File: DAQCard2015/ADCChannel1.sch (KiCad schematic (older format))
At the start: 50 parts, among them U1 LTC6403, U2 AD9219, U3 LTC6403, U4 LTC6403, U5 LTC6403

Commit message: Replaces single ample with 4-channel varients. Greatly reducing part count
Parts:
- removed C1, C15, C16: .01uF, symbol C
- removed C12, C13, C14, C17, C18, C19, C20, C21, C22: C, symbol C
- removed C8: 2.2uF, symbol CP
- removed C9: .1uF, symbol C
- removed R1, R13, R14: Rt, symbol R
- removed R11, R12, R19, R20, R21, R22: Rf, symbol R
- removed R15, R16, R17, R18, R2, R3: Ri, symbol R
- removed R23: 2.7k, symbol R
- removed R24: 1k, symbol R
- removed U1, U3, U4, U5: LTC6403, symbol LTC6403
- removed U2: AD9219, symbol AD9219
- added C8: .1uF, symbol C
- added C9: 2.2uF, symbol CP
- added R4: Rt, symbol R
- added RP1: R_PACK8, symbol R_PACK8
- added RP2, RP3: Rf, symbol R_PACK4
- added U2: THS4524IDBTR, symbol THS4524IDBTR
- added U3: AD9219, symbol AD9219
- C11: value .01uF -> .1uF
- C2, C3: value .1uF -> C
- C5: value C -> .01uF
- C6: value C -> .1uF
- R10: value Ri -> 10k
- R5, R6: value Rf -> Rt
- R7: value 10k -> Rt
- R8: value Rt -> 2.7k
- R9: value Ri -> 1k
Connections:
- net labels added: 3V3ana, VOCM
- net labels removed: 3V3, Vocm
- wire segments 178 -> 192
- no-connect marks 12 -> 4

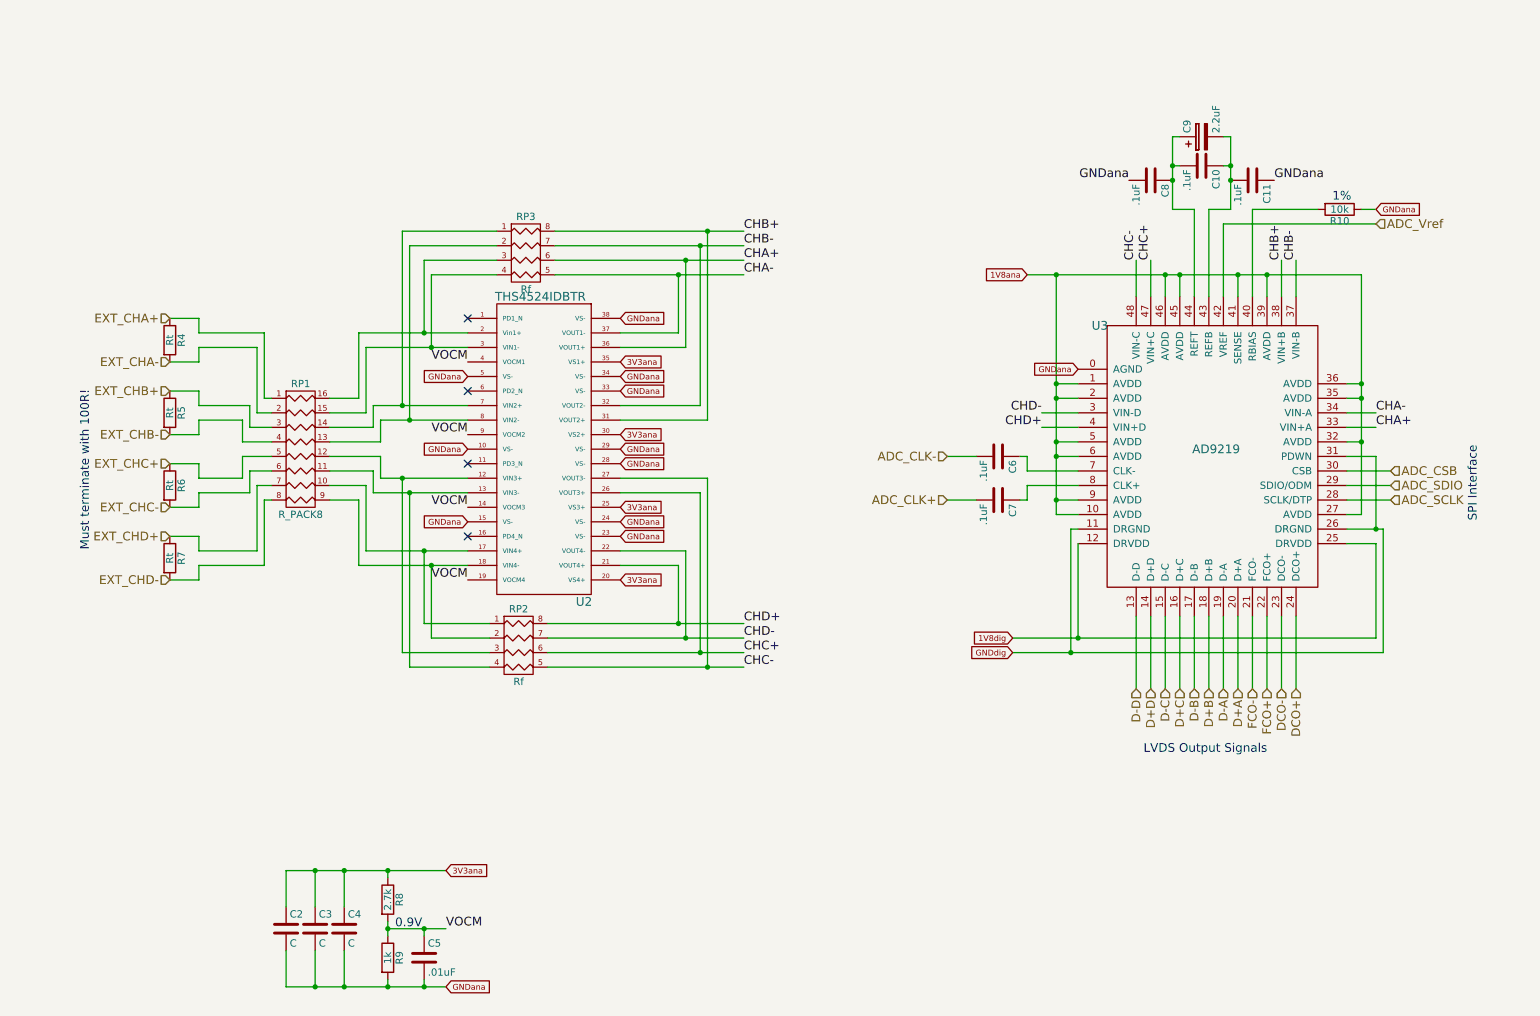
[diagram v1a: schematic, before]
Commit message: Finishes initial version of schematic(mostly). And adds a whole bunch of new footprints!
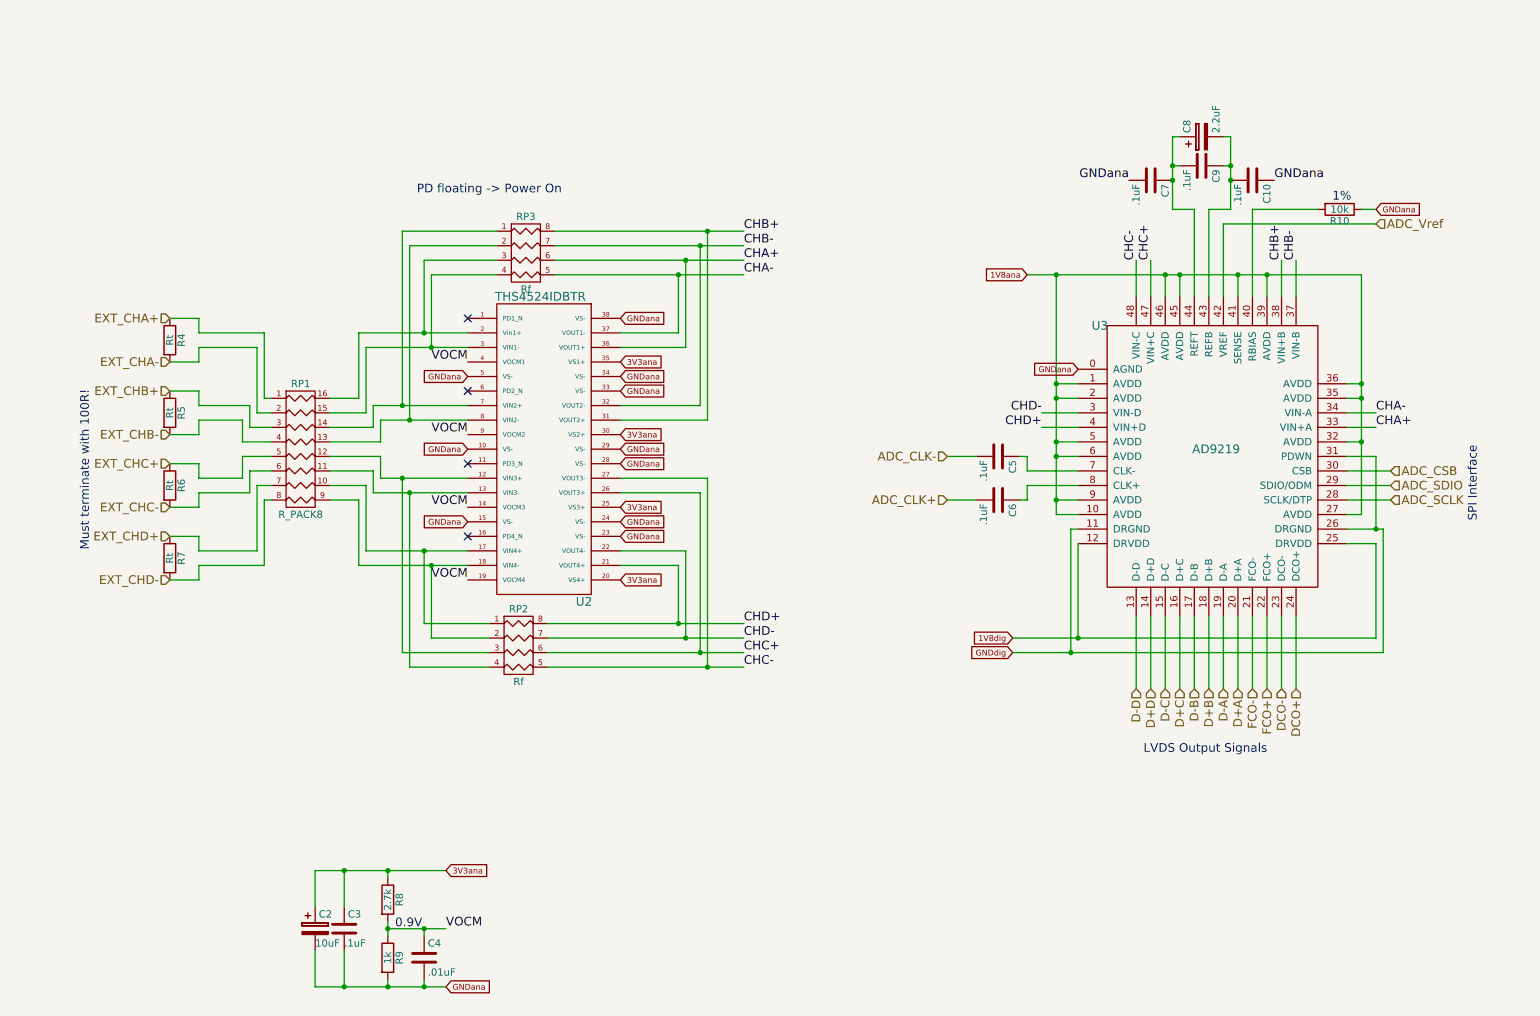
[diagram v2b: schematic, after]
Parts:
- removed C11, C8: .1uF, symbol C
- removed C2: C, symbol C
- removed C9: 2.2uF, symbol CP
- added C2: 10uF, extras:SMD_Cap_3mmDia, symbol CP
- added C8: 2.2uF, extras:SMD_Cap_3mmDia, symbol CP
- added C9: .1uF, Capacitors_SMD:C_0603, symbol C
- C10, C6, C7: footprint (none) -> Capacitors_SMD:C_0603
- C3: value C -> .1uF; footprint (none) -> Capacitors_SMD:C_0603
- C4: value C -> .01uF; footprint (none) -> Capacitors_SMD:C_0603
- C5: value .01uF -> .1uF; footprint (none) -> Capacitors_SMD:C_0603
- R10, R4, R5, R6, R7, R8, R9: footprint (none) -> Resistors_SMD:R_0603
- RP1: footprint (none) -> extras:R8_MNR18
- RP2, RP3: footprint (none) -> extras:R4-MNR04
- U2: footprint (none) -> Housings_SSOP:TSSOP-38_4.4x9.7mm_Pitch0.5mm
- U3: footprint (none) -> SMD_Packages:QFN-48-1EP
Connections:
- net 3V3ana: now also C2.1; no longer C4.1
- net ADC_CLK+: now also C6.2; no longer C7.2
- net ADC_CLK-: now also C5.2; no longer C6.2
- net GNDana: now also C10.1, C7.2, C2.2; no longer C5.2
- net VOCM: now also C4.1; no longer C5.1
- net at U3.8 (CLK+): now also C6.1; no longer C7.1
- net at U3.43 (REFB): now also C10.2, C8.2, C9.1; no longer C10.1
- net at U3.44 (REFT): now also C7.1, C8.1, C9.2; no longer C10.2
- net at U3.7 (CLK-): now also C5.1; no longer C6.1
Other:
- note added: "PD floating -> Power On"
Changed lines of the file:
@@
 $Comp
 L AD9219 U3
-U 1 1 55CFF5AD
+U 1 1 55CB5758
 P 9050 3700
 F 0 "U3" H 8250 4650 60  0000 C CNN
 F 1 "AD9219" H 9050 3800 60  0000 C CNN
-F 2 "" H 8650 3700 60  0000 C CNN
+F 2 "SMD_Packages:QFN-48-1EP" H 8650 3700 60  0001 C CNN
 F 3 "" H 8650 3700 60  0000 C CNN
 	1    9050 3700
@@
 $Comp
 L R R8
-U 1 1 55CFF5F5
+U 1 1 55CB5786
 P 3350 6700
 F 0 "R8" V 3430 6700 50  0000 C CNN
 F 1 "2.7k" V 3350 6700 50  0000 C CNN
-F 2 "" V 3280 6700 30  0000 C CNN
+F 2 "Resistors_SMD:R_0603" V 3280 6700 30  0001 C CNN
 F 3 "" H 3350 6700 30  0000 C CNN
 	1    3350 6700
@@
 $Comp
 L R R9
-U 1 1 55CFF5DE
+U 1 1 55CB577C
 P 3350 7100
 F 0 "R9" V 3430 7100 50  0000 C CNN
 F 1 "1k" V 3350 7100 50  0000 C CNN
-F 2 "" V 3280 7100 30  0000 C CNN
+F 2 "Resistors_SMD:R_0603" V 3280 7100 30  0001 C CNN
 F 3 "" H 3350 7100 30  0000 C CNN
 	1    3350 7100
@@
 Must terminate with 100R!
 $Comp
-L C C2
-U 1 1 55CFF5C9
-P 2650 6900
-F 0 "C2" H 2675 7000 50  0000 L CNN
-F 1 "C" H 2675 6800 50  0000 L CNN
-F 2 "" H 2688 6750 30  0000 C CNN
-F 3 "" H 2650 6900 60  0000 C CNN
-	1    2650 6900
-	1    0    0    -1
-$EndComp
-$Comp
 L C C3
-U 1 1 55CFF5B5
-P 2850 6900
-F 0 "C3" H 2875 7000 50  0000 L CNN
-F 1 "C" H 2875 6800 50  0000 L CNN
-F 2 "" H 2888 6750 30  0000 C CNN
-F 3 "" H 2850 6900 60  0000 C CNN
-	1    2850 6900
-	1    0    0    -1
-$EndComp
-$Comp
-L C C4
-U 1 1 55CFF5BB
+U 1 1 55CB575C
 P 3050 6900
-F 0 "C4" H 3075 7000 50  0000 L CNN
-F 1 "C" H 3075 6800 50  0000 L CNN
-F 2 "" H 3088 6750 30  0000 C CNN
+F 0 "C3" H 3075 7000 50  0000 L CNN
+F 1 ".1uF" H 3050 6800 50  0000 L CNN
+F 2 "Capacitors_SMD:C_0603" H 3088 6750 30  0001 C CNN
 F 3 "" H 3050 6900 60  0000 C CNN
 	1    3050 6900
@@
 ADC_SCLK
 $Comp
-L C C6
-U 1 1 55CFF5C6
+L C C5
+U 1 1 55CB5765
 P 7550 3650
-F 0 "C6" H 7575 3750 50  0000 L CNN
+F 0 "C5" H 7575 3750 50  0000 L CNN
 F 1 ".1uF" H 7575 3550 50  0000 L CNN
-F 2 "" H 7588 3500 30  0000 C CNN
+F 2 "Capacitors_SMD:C_0603" H 7588 3500 30  0001 C CNN
 F 3 "" H 7550 3650 60  0000 C CNN
 	1    7550 3650
@@
 $EndComp
 $Comp
-L C C7
-U 1 1 55CE4061
+L C C6
+U 1 1 55CB5746
 P 7550 3950
-F 0 "C7" H 7575 4050 50  0000 L CNN
+F 0 "C6" H 7575 4050 50  0000 L CNN
 F 1 ".1uF" H 7575 3850 50  0000 L CNN
-F 2 "" H 7588 3800 30  0000 C CNN
+F 2 "Capacitors_SMD:C_0603" H 7588 3800 30  0001 C CNN
 F 3 "" H 7550 3950 60  0000 C CNN
 	1    7550 3950
@@
 DCO+
 $Comp
-L C C11
-U 1 1 55CFF5FE
+L C C10
+U 1 1 55CB578F
 P 9300 1750
-F 0 "C11" H 9325 1850 50  0000 L CNN
+F 0 "C10" H 9325 1850 50  0000 L CNN
 F 1 ".1uF" H 9325 1650 50  0000 L CNN
-F 2 "" H 9338 1600 30  0000 C CNN
+F 2 "Capacitors_SMD:C_0603" H 9338 1600 30  0001 C CNN
 F 3 "" H 9300 1750 60  0000 C CNN
 	1    9300 1750
@@
 $EndComp
 $Comp
-L C C8
-U 1 1 55CFF5CE
+L C C7
+U 1 1 55CB5768
 P 8600 1750
-F 0 "C8" H 8625 1850 50  0000 L CNN
+F 0 "C7" H 8625 1850 50  0000 L CNN
 F 1 ".1uF" H 8625 1650 50  0000 L CNN
-F 2 "" H 8638 1600 30  0000 C CNN
+F 2 "Capacitors_SMD:C_0603" H 8638 1600 30  0001 C CNN
 F 3 "" H 8600 1750 60  0000 C CNN
 	1    8600 1750
@@
 $EndComp
 $Comp
-L C C10
-U 1 1 55CFF5D5
+L C C9
+U 1 1 55CB576F
 P 8950 1650
-F 0 "C10" H 8975 1750 50  0000 L CNN
+F 0 "C9" H 8975 1750 50  0000 L CNN
 F 1 ".1uF" H 8975 1550 50  0000 L CNN
-F 2 "" H 8988 1500 30  0000 C CNN
+F 2 "Capacitors_SMD:C_0603" H 8988 1500 30  0001 C CNN
 F 3 "" H 8950 1650 60  0000 C CNN
 	1    8950 1650
@@
 GNDana
 $Comp
-L CP C9
-U 1 1 55CFF600
+L CP C8
+U 1 1 55CB5792
 P 8950 1450
-F 0 "C9" H 8975 1550 50  0000 L CNN
+F 0 "C8" H 8975 1550 50  0000 L CNN
 F 1 "2.2uF" H 8975 1350 50  0000 L CNN
-F 2 "" H 8988 1300 30  0000 C CNN
+F 2 "extras:SMD_Cap_3mmDia" H 8988 1300 30  0001 C CNN
 F 3 "" H 8950 1450 60  0000 C CNN
 	1    8950 1450
@@
 $Comp
 L R R10
-U 1 1 55CFF5ED
+U 1 1 55CB5780
 P 9900 1950
 F 0 "R10" V 9980 1950 50  0000 C CNN
 F 1 "10k" V 9900 1950 50  0000 C CNN
-F 2 "" V 9830 1950 30  0000 C CNN
+F 2 "Resistors_SMD:R_0603" V 9830 1950 30  0001 C CNN
 F 3 "" H 9900 1950 30  0000 C CNN
 	1    9900 1950
@@
 $Comp
 L THS4524IDBTR U2
-U 1 1 55CFF606
+U 1 1 55CB579D
 P 4400 3700
 F 0 "U2" H 4700 2750 60  0000 C CNN
 F 1 "THS4524IDBTR" H 4400 4850 60  0000 C CNN
-F 2 "" H 4600 3800 60  0000 C CNN
+F 2 "Housings_SSOP:TSSOP-38_4.4x9.7mm_Pitch0.5mm" H 4600 3800 60  0001 C CNN
 F 3 "" H 4600 3800 60  0000 C CNN
 	1    4400 3700
@@
 $EndComp
 $Comp
-L C C5
-U 1 1 55CFF610
+L C C4
+U 1 1 55CB57A4
 P 3600 7100
-F 0 "C5" H 3625 7200 50  0000 L CNN
+F 0 "C4" H 3625 7200 50  0000 L CNN
 F 1 ".01uF" H 3625 7000 50  0000 L CNN
-F 2 "" H 3638 6950 30  0000 C CNN
+F 2 "Capacitors_SMD:C_0603" H 3638 6950 30  0001 C CNN
 F 3 "" H 3600 7100 60  0000 C CNN
 	1    3600 7100
@@
 Connection ~ 3600 6900
 Wire Wire Line
-	2650 6500 3750 6500
-Wire Wire Line
 	3050 6500 3050 6750
 Connection ~ 3350 6500
@@
 Connection ~ 3050 6500
 Wire Wire Line
-	2650 6500 2650 6750
-Connection ~ 2850 6500
-Wire Wire Line
-	2650 7300 3750 7300
-Wire Wire Line
 	3050 7300 3050 7050
 Wire Wire Line
 	2850 7300 2850 7050
 Connection ~ 3050 7300
-Wire Wire Line
-	2650 7300 2650 7050
-Connection ~ 2850 7300
 Wire Wire Line
 	3600 7300 3600 7250
@@
 $Comp
 L R R7
-U 1 1 55CFF61A
+U 1 1 55CB57A8
 P 1850 4350
 F 0 "R7" V 1930 4350 50  0000 C CNN
 F 1 "Rt" V 1850 4350 50  0000 C CNN
-F 2 "" V 1780 4350 30  0000 C CNN
+F 2 "Resistors_SMD:R_0603" V 1780 4350 30  0001 C CNN
 F 3 "" H 1850 4350 30  0000 C CNN
 	1    1850 4350
@@
 $Comp
 L R R6
-U 1 1 55CFF61B
+U 1 1 55CB57B1
 P 1850 3850
 F 0 "R6" V 1930 3850 50  0000 C CNN
 F 1 "Rt" V 1850 3850 50  0000 C CNN
-F 2 "" V 1780 3850 30  0000 C CNN
+F 2 "Resistors_SMD:R_0603" V 1780 3850 30  0001 C CNN
 F 3 "" H 1850 3850 30  0000 C CNN
 	1    1850 3850
@@
 $Comp
 L R R5
-U 1 1 55CFF628
+U 1 1 55CB57B5
 P 1850 3350
 F 0 "R5" V 1930 3350 50  0000 C CNN
 F 1 "Rt" V 1850 3350 50  0000 C CNN
-F 2 "" V 1780 3350 30  0000 C CNN
+F 2 "Resistors_SMD:R_0603" V 1780 3350 30  0001 C CNN
 F 3 "" H 1850 3350 30  0000 C CNN
 	1    1850 3350
@@
 $Comp
 L R R4
-U 1 1 55CFF62E
+U 1 1 55CB57BD
 P 1850 2850
 F 0 "R4" V 1930 2850 50  0000 C CNN
 F 1 "Rt" V 1850 2850 50  0000 C CNN
-F 2 "" V 1780 2850 30  0000 C CNN
+F 2 "Resistors_SMD:R_0603" V 1780 2850 30  0001 C CNN
 F 3 "" H 1850 2850 30  0000 C CNN
 	1    1850 2850
@@
 $Comp
 L R_PACK4 RP2
-U 1 1 55CFF632
+U 1 1 55CB57C4
 P 4250 5150
 F 0 "RP2" H 4250 5600 50  0000 C CNN
 F 1 "Rf" H 4250 5100 50  0000 C CNN
-F 2 "" H 4250 5150 60  0000 C CNN
+F 2 "extras:R4-MNR04" H 4250 5150 60  0001 C CNN
 F 3 "" H 4250 5150 60  0000 C CNN
 	1    4250 5150
@@
 $Comp
 L R_PACK4 RP3
-U 1 1 55CF51DE
+U 1 1 55CB574C
 P 4300 2450
 F 0 "RP3" H 4300 2900 50  0000 C CNN
 F 1 "Rf" H 4300 2400 50  0000 C CNN
-F 2 "" H 4300 2450 60  0000 C CNN
+F 2 "extras:R4-MNR04" H 4300 2450 60  0001 C CNN
 F 3 "" H 4300 2450 60  0000 C CNN
 	1    4300 2450
@@
 $Comp
 L R_PACK8 RP1
-U 1 1 55CFF641
+U 1 1 55CB57CA
 P 2750 3600
 F 0 "RP1" H 2750 4050 50  0000 C CNN
 F 1 "R_PACK8" H 2750 3150 50  0000 C CNN
-F 2 "" H 2750 3600 60  0000 C CNN
+F 2 "extras:R8_MNR18" H 2750 3600 60  0001 C CNN
 F 3 "" H 2750 3600 60  0000 C CNN
 	1    2750 3600
@@
 Text GLabel 10150 1950 2    40   Input ~ 0
 GNDana
+Wire Wire Line
+	3750 6500 2850 6500
+Wire Wire Line
+	2850 7300 3750 7300
+$Comp
+L CP C2
+U 1 1 55CB2D9D
+P 2850 6900
+F 0 "C2" H 2875 7000 50  0000 L CNN
+F 1 "10uF" H 2850 6800 50  0000 L CNN
+F 2 "extras:SMD_Cap_3mmDia" H 2888 6750 30  0001 C CNN
+F 3 "" H 2850 6900 60  0000 C CNN
+	1    2850 6900
+	1    0    0    -1
+$EndComp
+Text Notes 3550 1850 0    60   ~ 0
+PD floating -> Power On
 $EndSCHEMATC

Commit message: Adds a more-or-less complete BOM to DAQ Card
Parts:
- C4: value .01uF -> 10000pF
- RP1: value R_PACK8 -> Ri
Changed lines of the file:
@@
 P 3600 7100
 F 0 "C4" H 3625 7200 50  0000 L CNN
-F 1 ".01uF" H 3625 7000 50  0000 L CNN
+F 1 "10000pF" H 3625 7000 50  0000 L CNN
 F 2 "Capacitors_SMD:C_0603" H 3638 6950 30  0001 C CNN
 F 3 "" H 3600 7100 60  0000 C CNN
@@
 P 2750 3600
 F 0 "RP1" H 2750 4050 50  0000 C CNN
-F 1 "R_PACK8" H 2750 3150 50  0000 C CNN
+F 1 "Ri" H 2750 3150 50  0000 C CNN
 F 2 "extras:R8_MNR18" H 2750 3600 60  0001 C CNN
 F 3 "" H 2750 3600 60  0000 C CNN

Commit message: Updates to DAQCard2015, especially to power systems
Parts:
- removed C2: 10uF, extras:SMD_Cap_3mmDia, symbol CP
- removed C3: .1uF, Capacitors_SMD:C_0603, symbol C
- removed C4: 10000pF, Capacitors_SMD:C_0603, symbol C
- removed C8: 2.2uF, extras:SMD_Cap_3mmDia, symbol CP
- removed R8: 2.7k, Resistors_SMD:R_0603, symbol R
- removed R9: 1k, Resistors_SMD:R_0603, symbol R
- added C8: 2.2uF, symbol C
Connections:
- net GNDdig is gone; now on net GND: U3.11 (DRGND), U3.26 (DRGND), U3.31 (PDWN)
- net at RP1.14 (R3), U2.7 (VIN2+): now also RP3.3 (P3); no longer RP3.1 (P1)
- net at RP1.13 (R4), U2.8 (VIN2-): now also RP3.4 (P4); no longer RP3.2 (P2)
- net at RP1.16 (R1), U2.2 (Vin1+): now also RP3.1 (P1); no longer RP3.3 (P3)
- net at RP1.15 (R2), U2.3 (VIN1-): now also RP3.2 (P2); no longer RP3.4 (P4)
- net at C10.2, C9.1, U3.43 (REFB): now also C8.2
- net at C7.1, C9.2, U3.44 (REFT): now also C8.1
- net at RP1.12 (R5), U2.12 (VIN3+): now also RP2.1 (P1); no longer RP2.3 (P3)
- net at RP1.11 (R6), U2.13 (VIN3-): now also RP2.2 (P2); no longer RP2.4 (P4)
- net at RP1.10 (R7), U2.17 (VIN4+): now also RP2.3 (P3); no longer RP2.1 (P1)
- net at RP1.9 (R8), U2.18 (VIN4-): now also RP2.4 (P4); no longer RP2.2 (P2)
- net GNDana renamed GND
- net VOCM renamed Vocm
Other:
- note removed: "0.9V"
